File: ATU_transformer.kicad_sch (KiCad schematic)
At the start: 175 parts, among them J14 Conn_Coaxial, J16 Conn_Coaxial, J2 Conn_01x03, K1 G2R-1-E DC12, K10 G2R-1-E DC12, K11 G2R-1-E DC12, K12 G2R-1-E DC12, K13 G2R-1-E DC12, K14 G2R-1-E DC12, K15 G2R-1-E DC12, K16 G2R-1-E DC12, K17 G2R-1-E DC12, K2 G2R-1-E DC12, K3 G2R-1-E DC12, K4 G2R-1-E DC12, K5 G2R-1-E DC12, K6 G2R-1-E DC12, K7 G2R-1-E DC12, K8 G2R-1-E DC12, K9 G2R-1-E DC12, T1 CST1, T2 CST1, U1 LM358

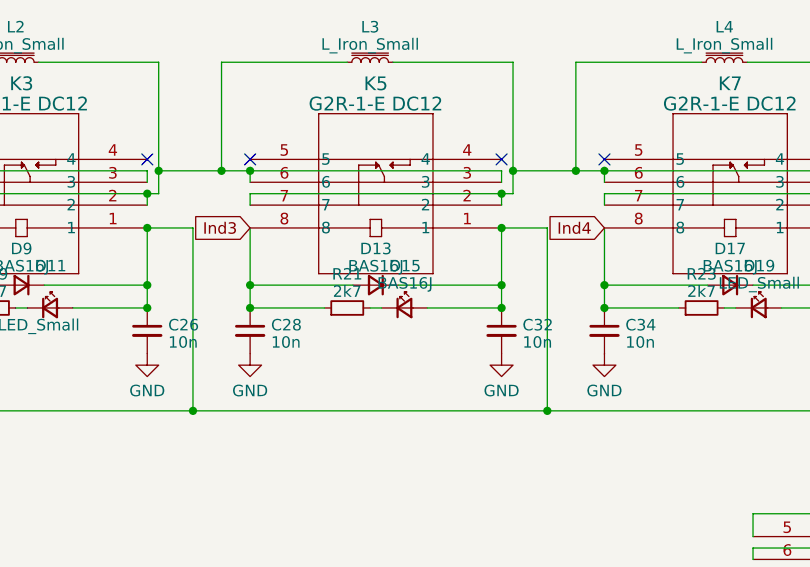
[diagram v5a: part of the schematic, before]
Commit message: placement F_Cu complete, starting B_Cu
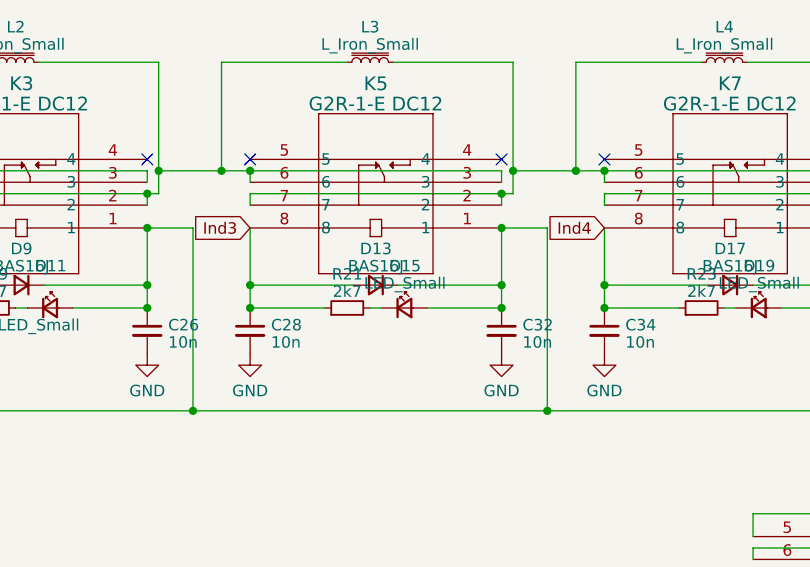
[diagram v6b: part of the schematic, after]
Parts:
- D15: value BAS16J -> LED_Small; footprint Diode_SMD:D_SOD-323_HandSoldering -> LED_SMD:LED_1206_3216Metric_Pad1.42x1.75mm_HandSolder
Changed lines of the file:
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@@
       (effects (font (size 1.27 1.27)))
     )
-    (property "Value" "BAS16J" (at 175.9585 56.9501 0)
+    (property "Value" "LED_Small" (at 175.9585 56.9501 0)
       (effects (font (size 1.27 1.27)))
     )
-    (property "Footprint" "Diode_SMD:D_SOD-323_HandSoldering" (at 175.895 59.69 90)
+    (property "Footprint" "LED_SMD:LED_1206_3216Metric_Pad1.42x1.75mm_HandSolder" (at 175.895 59.69 90)
       (effects (font (size 1.27 1.27)) hide)
     )

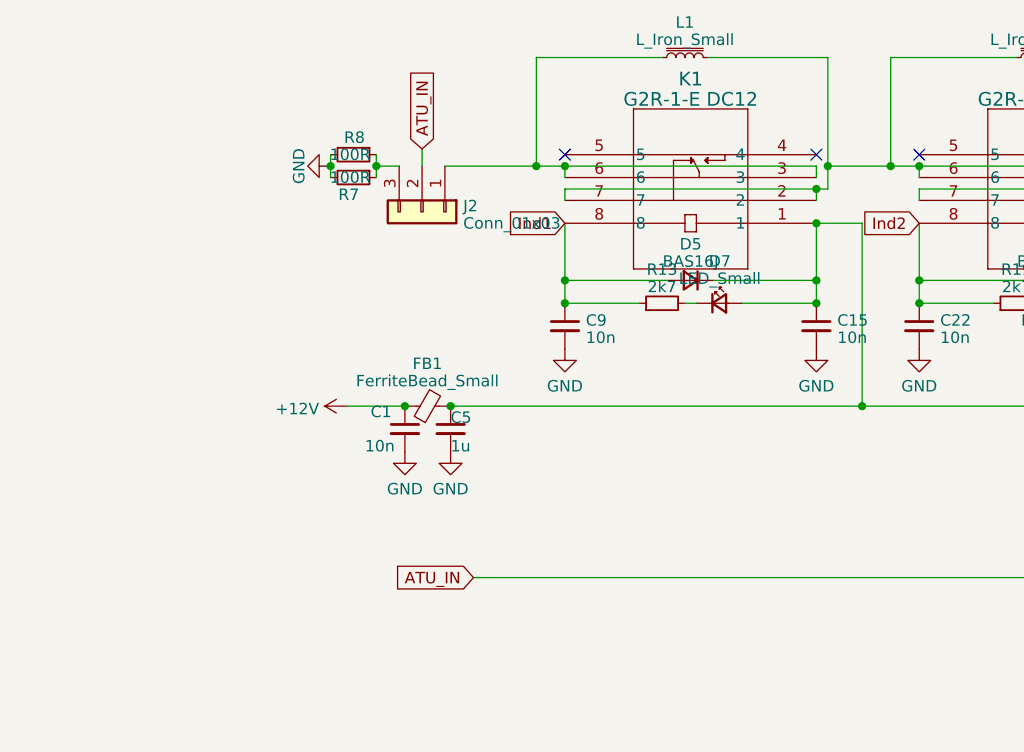
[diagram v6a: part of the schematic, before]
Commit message: more passive component layout, new silkscreen
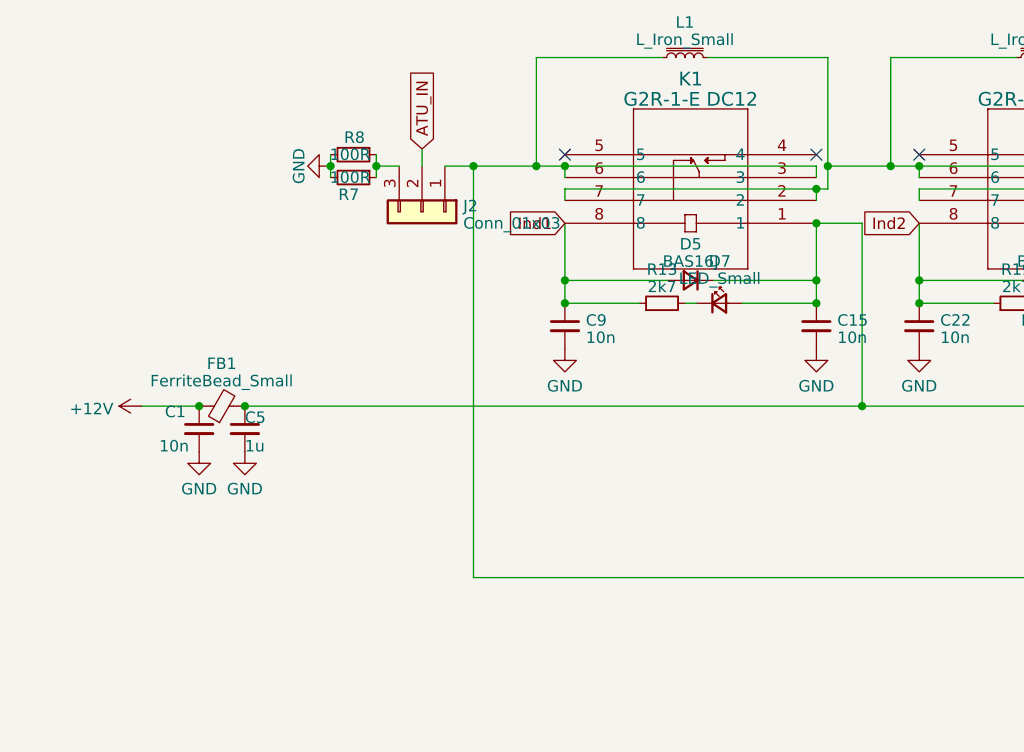
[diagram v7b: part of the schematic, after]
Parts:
- L1, L2, L3, L4, L5, L6, L7, L8: footprint Inductor_THT:L_Toroid_Horizontal_D25.4mm_P22.90mm_Vishay_TJ5_BigPads -> L_Toroid_Horizontal_D25.4mm_P22.90mm:L_Toroid_Horizontal_25x22
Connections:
- net ATU_IN: no longer C12.2, C25.2, C31.2, C37.2, C45.2, C51.2, C57.2, C63.2, K9.2, K9.7
- net at J2.1 (Pin_1), K1.3, K1.6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: now also C12.2, C25.2, C31.2, C37.2, C45.2, C51.2, C57.2, C63.2, K9.2, K9.7
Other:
- moved on the sheet: C1, C5, FB1

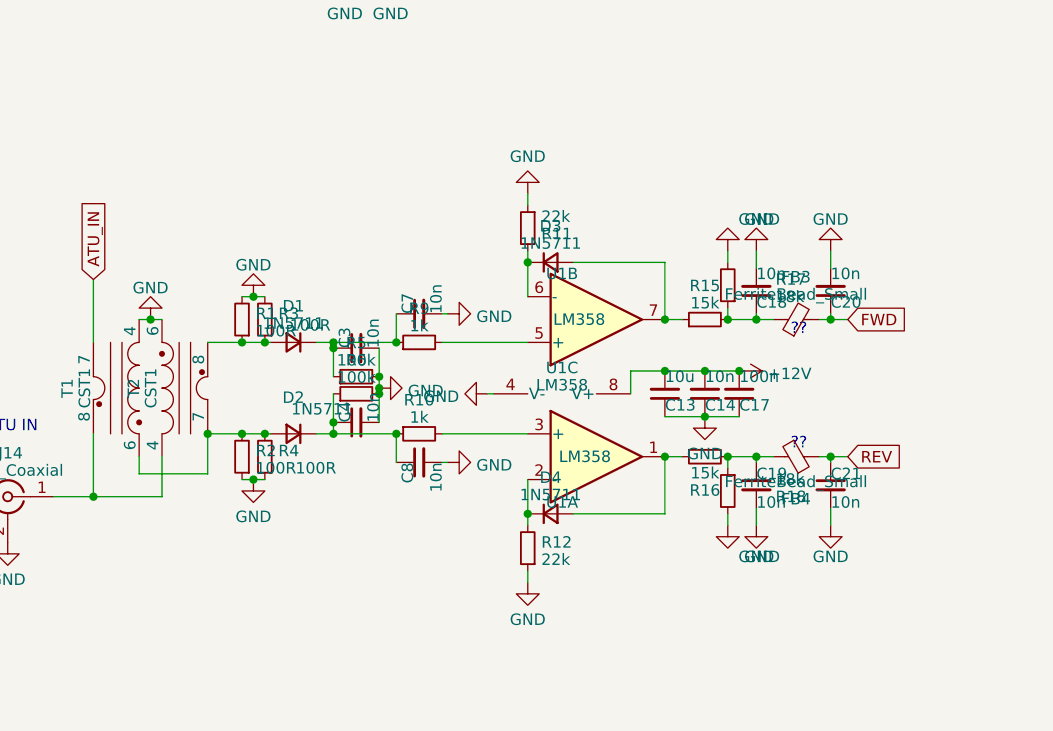
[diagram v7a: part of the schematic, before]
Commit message: all components are placed
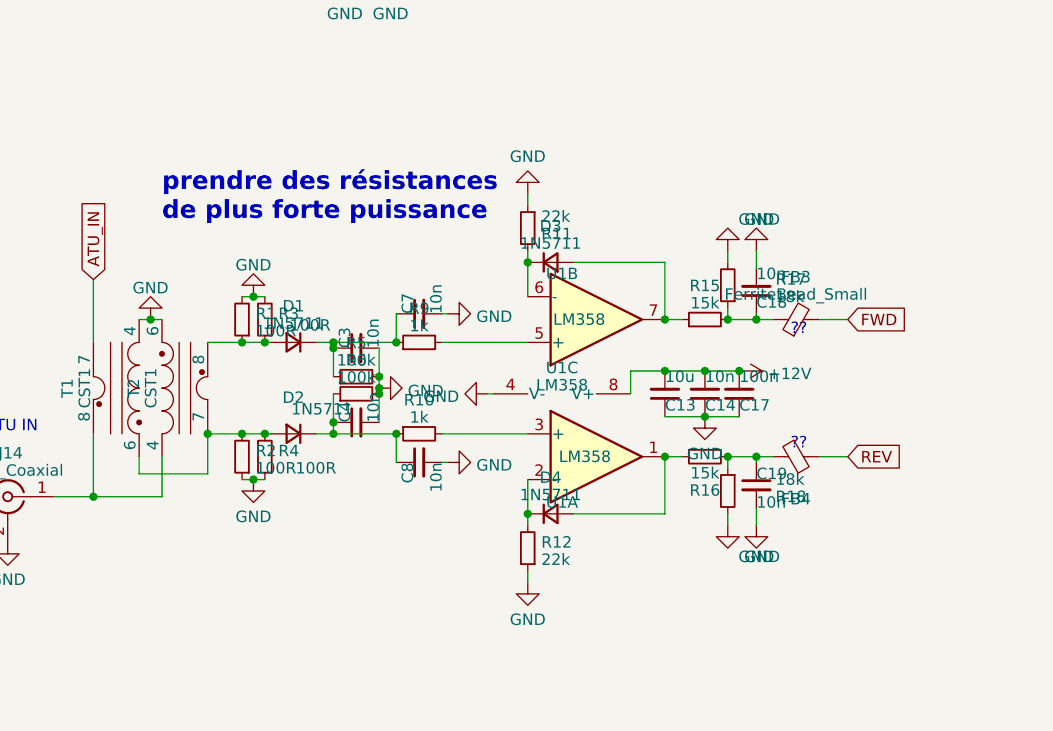
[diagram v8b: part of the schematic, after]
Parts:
- removed C20, C21: 10n, Capacitor_SMD:C_0805_2012Metric_Pad1.18x1.45mm_HandSolder, symbol Device:C_Small
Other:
- note added: "prendre des résistances de plus forte puissance"
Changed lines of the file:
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@@
   (junction (at 119.38 44.45) (diameter 0) (color 0 0 0 0)
   )
-  (junction (at 118.11 220.345) (diameter 0) (color 0 0 0 0)
-  )
   (junction (at 344.17 139.065) (diameter 0) (color 0 0 0 0)
   )
@@
   (junction (at 214.63 90.17) (diameter 0) (color 0 0 0 0)
   )
-  (junction (at 118.11 205.105) (diameter 0) (color 0 0 0 0)
-  )
   (junction (at 119.38 59.69) (diameter 0) (color 0 0 0 0)
   )
@@
     (stroke (width 0) (type default))
   )
-  (wire (pts (xy 118.11 204.47) (xy 118.11 205.105))
-    (stroke (width 0) (type default))
-  )
   (wire (pts (xy 384.81 32.385) (xy 371.475 32.385))
     (stroke (width 0) (type default))
@@
     (stroke (width 0) (type default))
   )
-  (wire (pts (xy 118.11 220.98) (xy 118.11 220.345))
-    (stroke (width 0) (type default))
-  )
   (wire (pts (xy 266.7 44.45) (xy 266.7 32.385))
     (stroke (width 0) (type default))
@@
     (stroke (width 0) (type default))
   )
-  (wire (pts (xy 118.11 220.345) (xy 120.015 220.345))
-    (stroke (width 0) (type default))
-  )
   (wire (pts (xy 344.17 46.99) (xy 345.44 46.99))
     (stroke (width 0) (type default))
@@
     (stroke (width 0) (type default))
   )
-  (wire (pts (xy 118.11 227.965) (xy 118.11 226.06))
-    (stroke (width 0) (type default))
-  )
   (wire (pts (xy 163.83 121.285) (xy 165.1 121.285))
     (stroke (width 0) (type default))
@@
     (stroke (width 0) (type default))
   )
-  (wire (pts (xy 116.84 220.345) (xy 118.11 220.345))
+  (wire (pts (xy 116.84 220.345) (xy 120.015 220.345))
     (stroke (width 0) (type default))
   )
@@
     (stroke (width 0) (type default))
   )
-  (wire (pts (xy 118.11 205.105) (xy 120.015 205.105))
+  (wire (pts (xy 116.84 205.105) (xy 120.015 205.105))
     (stroke (width 0) (type default))
   )
@@
     (stroke (width 0) (type default))
   )
-  (wire (pts (xy 118.11 197.485) (xy 118.11 199.39))
-    (stroke (width 0) (type default))
-  )
   (wire (pts (xy 266.7 44.45) (xy 273.685 44.45))
     (stroke (width 0) (type default))
@@
     (stroke (width 0) (type default))
   )
-  (wire (pts (xy 116.84 205.105) (xy 118.11 205.105))
-    (stroke (width 0) (type default))
-  )
   (wire (pts (xy 147.32 145.415) (xy 147.32 149.225))
     (stroke (width 0) (type default))
@@
     (stroke (width 0) (type default))
   )
+  (text "prendre des résistances \nde plus forte puissance" (at 43.815 194.31 0)
+    (effects (font (size 2 2) (thickness 0.4) bold) (justify left bottom))
+  )
   (text "??" (at 113.665 219.71 0)
     (effects (font (size 1.27 1.27)) (justify left bottom))
@@
     )
   )
-  (symbol (lib_id "power:GND") (at 118.11 227.965 0) (mirror y) (unit 1)
-    (in_bom yes) (on_board yes) (dnp no) (fields_autoplaced)
-    (property "Reference" "#PWR030" (at 118.11 234.315 0)
-      (effects (font (size 1.27 1.27)) hide)
-    )
-    (property "Value" "GND" (at 118.11 231.4669 0)
-      (effects (font (size 1.27 1.27)))
-    )
-    (property "Footprint" "" (at 118.11 227.965 0)
-      (effects (font (size 1.27 1.27)) hide)
-    )
-    (property "Datasheet" "" (at 118.11 227.965 0)
-      (effects (font (size 1.27 1.27)) hide)
-    )
-    (pin "1")
-    (instances
-      (project "K_Aries"
-        (path "/4d56c8f7-829b-457e-80cb-74e9f55628bb/d6e8d14c-e765-45cf-852c-f558c754ac0c"
-          (reference "#PWR030") (unit 1)
-        )
-      )
-    )
-  )
   (symbol (lib_id "power:GND") (at 214.63 106.68 0) (unit 1)
     (in_bom yes) (on_board yes) (dnp no) (fields_autoplaced)
@@
     )
     (property "Value" "FerriteBead_Small" (at 114.2619 223.1357 90)
-      (effects (font (size 1.27 1.27)))
+      (effects (font (size 1.27 1.27)) hide)
     )
     (property "Footprint" "Inductor_SMD:L_0805_2012Metric_Pad1.15x1.40mm_HandSolder" (at 114.3 218.567 90)
@@
     )
   )
-  (symbol (lib_id "power:GND") (at 118.11 197.485 180) (unit 1)
-    (in_bom yes) (on_board yes) (dnp no) (fields_autoplaced)
-    (property "Reference" "#PWR029" (at 118.11 191.135 0)
-      (effects (font (size 1.27 1.27)) hide)
-    )
-    (property "Value" "GND" (at 118.11 193.9831 0)
-      (effects (font (size 1.27 1.27)))
-    )
-    (property "Footprint" "" (at 118.11 197.485 0)
-      (effects (font (size 1.27 1.27)) hide)
-    )
-    (property "Datasheet" "" (at 118.11 197.485 0)
-      (effects (font (size 1.27 1.27)) hide)
-    )
-    (pin "1")
-    (instances
-      (project "K_Aries"
-        (path "/4d56c8f7-829b-457e-80cb-74e9f55628bb/d6e8d14c-e765-45cf-852c-f558c754ac0c"
-          (reference "#PWR029") (unit 1)
-        )
-      )
-    )
-  )
   (symbol (lib_id "Device:C_Small") (at 80.01 151.765 0) (unit 1)
     (in_bom yes) (on_board yes) (dnp no) (fields_autoplaced)
@@
     )
   )
-  (symbol (lib_id "Device:C_Small") (at 118.11 201.93 0) (mirror x) (unit 1)
-    (in_bom yes) (on_board yes) (dnp no)
-    (property "Reference" "C20" (at 118.11 203.2 0)
-      (effects (font (size 1.27 1.27)) (justify left))
-    )
-    (property "Value" "10n" (at 118.11 200.025 0)
-      (effects (font (size 1.27 1.27)) (justify left))
-    )
-    (property "Footprint" "Capacitor_SMD:C_0805_2012Metric_Pad1.18x1.45mm_HandSolder" (at 118.11 201.93 0)
-      (effects (font (size 1.27 1.27)) hide)
-    )
-    (property "Datasheet" "~" (at 118.11 201.93 0)
-      (effects (font (size 1.27 1.27)) hide)
-    )
-    (pin "1")
-    (pin "2")
-    (instances
-      (project "K_Aries"
-        (path "/4d56c8f7-829b-457e-80cb-74e9f55628bb/d6e8d14c-e765-45cf-852c-f558c754ac0c"
-          (reference "C20") (unit 1)
-        )
-      )
-    )
-  )
   (symbol (lib_id "Device:D_Small") (at 86.995 198.755 0) (unit 1)
     (in_bom yes) (on_board yes) (dnp no) (fields_autoplaced)
@@
         )
       )
-    )
-  )
-  (symbol (lib_id "Device:C_Small") (at 118.11 223.52 0) (unit 1)
-    (in_bom yes) (on_board yes) (dnp no)
-    (property "Reference" "C21" (at 118.11 222.25 0)
-      (effects (font (size 1.27 1.27)) (justify left))
-    )
-    (property "Value" "10n" (at 118.11 225.425 0)
-      (effects (font (size 1.27 1.27)) (justify left))
-    )
-    (property "Footprint" "Capacitor_SMD:C_0805_2012Metric_Pad1.18x1.45mm_HandSolder" (at 118.11 223.52 0)
-      (effects (font (size 1.27 1.27)) hide)
-    )
-    (property "Datasheet" "~" (at 118.11 223.52 0)
-      (effects (font (size 1.27 1.27)) hide)
-    )
-    (pin "1")
-    (pin "2")
-    (instances
-      (project "K_Aries"
-        (path "/4d56c8f7-829b-457e-80cb-74e9f55628bb/d6e8d14c-e765-45cf-852c-f558c754ac0c"
-          (reference "C21") (unit 1)
-        )
-      )
